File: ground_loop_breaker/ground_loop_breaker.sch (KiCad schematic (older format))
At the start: 0 parts

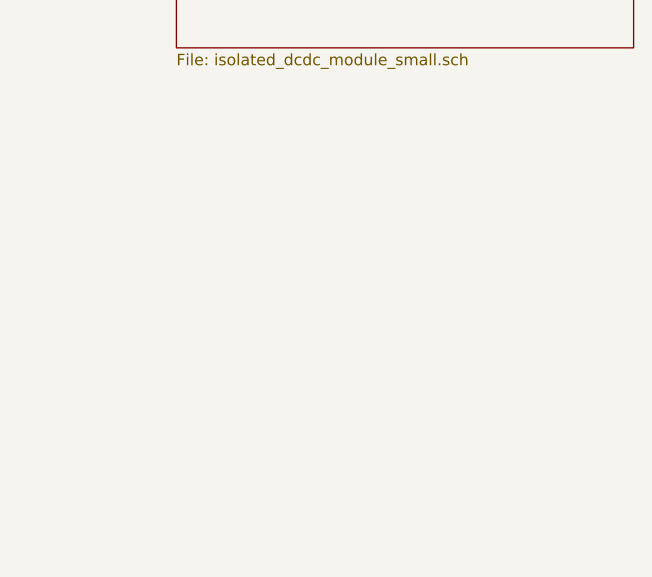
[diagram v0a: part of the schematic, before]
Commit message: ground loop breaker fin
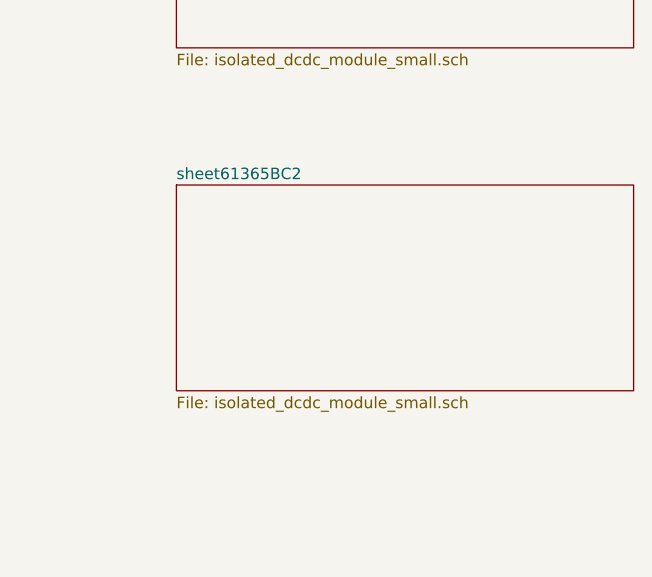
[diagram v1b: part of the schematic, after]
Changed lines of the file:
@@
 F1 "isolated_dcdc_module.sch" 50
 $EndSheet
+$Sheet
+S 5400 2700 2000 900
+U 61365BC4
+F0 "sheet61365BC2" 50
+F1 "isolated_dcdc_module_small.sch" 50
+$EndSheet
 $EndSCHEMATC
